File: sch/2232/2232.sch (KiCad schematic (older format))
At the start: 70 parts, among them J1 47346-0001, J2 IDC-06, J3 IDC-06, J4 IDC-10, J5 IDC-10, J6 6P6C, J7 Screw_Terminal_01x06, J8 Screw_Terminal_01x06, Q1 Q_NPN_BEC, Q2 Q_NPN_BEC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

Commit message: RN remap
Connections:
- net EEDATA: now also RN3.9 (R8); no longer RN3.2 (R2)
- net ISP_MISO: now also RN3.1 (R1); no longer RN3.3 (R3)
- net ISP_RST: now also RN3.2 (R2); no longer RN3.4 (R4)
- net MCU_BUFF: now also RN3.3 (R3); no longer RN3.8 (R7)
- net MCU_RST: now also RN3.4 (R4); no longer RN3.9 (R8)
- net USB_reset: now also RN3.8 (R7); no longer RN3.1 (R1)
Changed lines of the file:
@@
 	1    0    0    -1
 $EndComp
-Text Label 4900 9200 3    50   ~ 0
+Text Label 5500 9200 3    50   ~ 0
 USB_reset
 $Comp
@@
 Text Label 2500 6650 2    50   ~ 0
 EEDATA
-Text Label 5000 9200 3    50   ~ 0
+Text Label 5600 9200 3    50   ~ 0
 EEDATA
 $Comp
@@
 Text Label 9250 3800 0    50   ~ 0
 ISP_MOSI
-Text Label 5100 9200 3    50   ~ 0
+Text Label 4900 9200 3    50   ~ 0
 ISP_MISO
-Text Label 5200 9200 3    50   ~ 0
+Text Label 5000 9200 3    50   ~ 0
 ISP_RST
 Text Label 5300 9200 3    50   ~ 0
@@
 Text Label 5400 9200 3    50   ~ 0
 FBUFF
-Text Label 5500 9200 3    50   ~ 0
+Text Label 5100 9200 3    50   ~ 0
 MCU_BUFF
 Text Label 6300 6150 2    50   ~ 0
 MCU_RST
 NoConn ~ 6300 6350
-Text Label 5600 9200 3    50   ~ 0
+Text Label 5200 9200 3    50   ~ 0
 MCU_RST
 Text Label 5400 10400 2    50   ~ 0

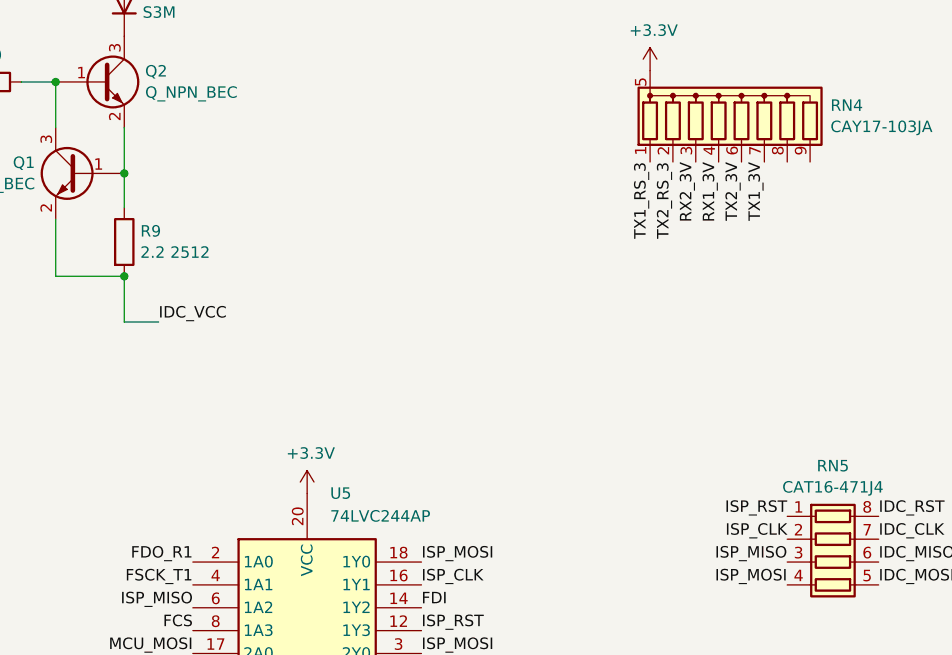
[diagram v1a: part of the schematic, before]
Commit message: All footprinted elements are routed
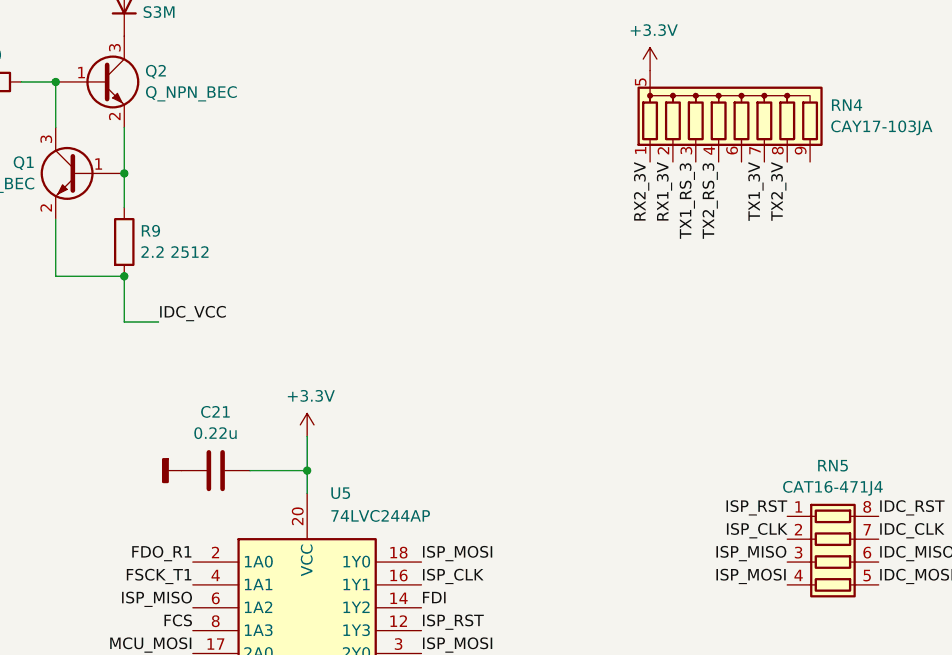
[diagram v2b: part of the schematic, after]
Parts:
- added C21: 0.22u, NevaDA:C_0603, symbol Device:C
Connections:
- net +3V3: now also C21.1
- net GNDD: now also C21.2
- net RX1_3V: now also RN4.2 (R2); no longer RN4.4 (R4)
- net RX2_3V: now also RN4.1 (R1); no longer RN4.3 (R3)
- net TX1_RS_3: now also RN4.3 (R3); no longer RN4.1 (R1)
- net TX2_3V: now also RN4.8 (R7); no longer RN4.6 (R5)
- net TX2_RS_3: now also RN4.4 (R4); no longer RN4.2 (R2)
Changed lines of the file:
@@
 	1    0    0    -1
 $EndComp
-Text Label 10350 2050 3    50   ~ 0
+Text Label 10550 2050 3    50   ~ 0
 TX2_RS_3
-Text Label 10250 2050 3    50   ~ 0
+Text Label 10450 2050 3    50   ~ 0
 TX1_RS_3
 Text Label 10750 2050 3    50   ~ 0
 TX1_3V
-Text Label 10650 2050 3    50   ~ 0
+Text Label 10850 2050 3    50   ~ 0
 TX2_3V
-Text Label 10550 2050 3    50   ~ 0
+Text Label 10350 2050 3    50   ~ 0
 RX1_3V
-Text Label 10450 2050 3    50   ~ 0
+Text Label 10250 2050 3    50   ~ 0
 RX2_3V
 Text Label 4300 4250 0    50   ~ 0
@@
 L power:+3.3V #PWR0130
 U 1 1 5FDED2D5
-P 8750 3500
-F 0 "#PWR0130" H 8750 3350 50  0001 C CNN
-F 1 "+3.3V" H 8765 3675 50  0000 C CNN
-F 2 "" H 8750 3500 50  0001 C CNN
-F 3 "" H 8750 3500 50  0001 C CNN
-	1    8750 3500
+P 8750 3250
+F 0 "#PWR0130" H 8750 3100 50  0001 C CNN
+F 1 "+3.3V" H 8765 3425 50  0000 C CNN
+F 2 "" H 8750 3250 50  0001 C CNN
+F 3 "" H 8750 3250 50  0001 C CNN
+	1    8750 3250
 	1    0    0    -1
 $EndComp
@@
 Text Label 7500 8150 0    50   ~ 0
 EN_UART
+$Comp
+L Device:C C21
+U 1 1 600B3D78
+P 8350 3400
+F 0 "C21" V 8095 3400 50  0000 C CNN
+F 1 "0.22u" V 8188 3400 50  0000 C CNN
+F 2 "NevaDA:C_0603" H 8388 3250 50  0001 C CNN
+F 3 "~" H 8350 3400 50  0001 C CNN
+	1    8350 3400
+	0    1    1    0
+$EndComp
+$Comp
+L power:GNDD #PWR0164
+U 1 1 600B3D90
+P 8200 3400
+F 0 "#PWR0164" H 8200 3150 50  0001 C CNN
+F 1 "GNDD" V 8204 3290 50  0001 R CNN
+F 2 "" H 8200 3400 50  0001 C CNN
+F 3 "" H 8200 3400 50  0001 C CNN
+	1    8200 3400
+	0    1    1    0
+$EndComp
+Wire Wire Line
+	8500 3400 8750 3400
+Wire Wire Line
+	8750 3250 8750 3400
+Connection ~ 8750 3400
+Wire Wire Line
+	8750 3400 8750 3500
 $EndSCHEMATC

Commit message: VCC routed
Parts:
- removed D10: S3M, symbol Device:D
- added D10: SMBJ5.0A-E3/52, NevaDA:DO-214AA_SMB, symbol Device:D_Zener
- added R11, R12, R13: 100, NevaDA:R_0603, symbol Device:R
- Q1: value Q_NPN_BEC -> BC817-40; footprint (none) -> NevaDA:SOT-23
- Q2: value Q_NPN_BEC -> FZT1049A; footprint (none) -> NevaDA:SOT-223; symbol Device:Q_NPN_BEC -> Device:Q_NPN_BCE
- R8: footprint (none) -> NevaDA:R_0603
- R9: value 2.2 2512 -> 1 1206; footprint (none) -> NevaDA:R_1206
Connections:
- net +3V3: now also R11.1
- net +5V: now also Q2.2 (C), R13.1
- net GNDD: now also D10.2 (A), R12.2
- net IDC_VCC: now also D10.1 (K)
- net at Q1.3 (C), Q2.1 (B), R8.1: now also R13.2
- net at Q1.1 (B), R9.1: now also Q2.3 (E); no longer Q2.2 (E)
- new net: R11.2, R12.1
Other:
- moved on the sheet: C21, Q1, Q2, R8, R9, RN5, U5
